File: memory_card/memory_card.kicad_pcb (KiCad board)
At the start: 2 copper layers, 100 x 100 mm, 22 parts, among them IC1 SN74HCT138N, IC2 SN74HCT138N, J1 Conn1, U1 AS6C4008, U2 74HCT374, U3 74HCT32, U4 74HCT00, U5 ZIF_AT28CXXX, U6 74HCT04, U7 74HCT374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

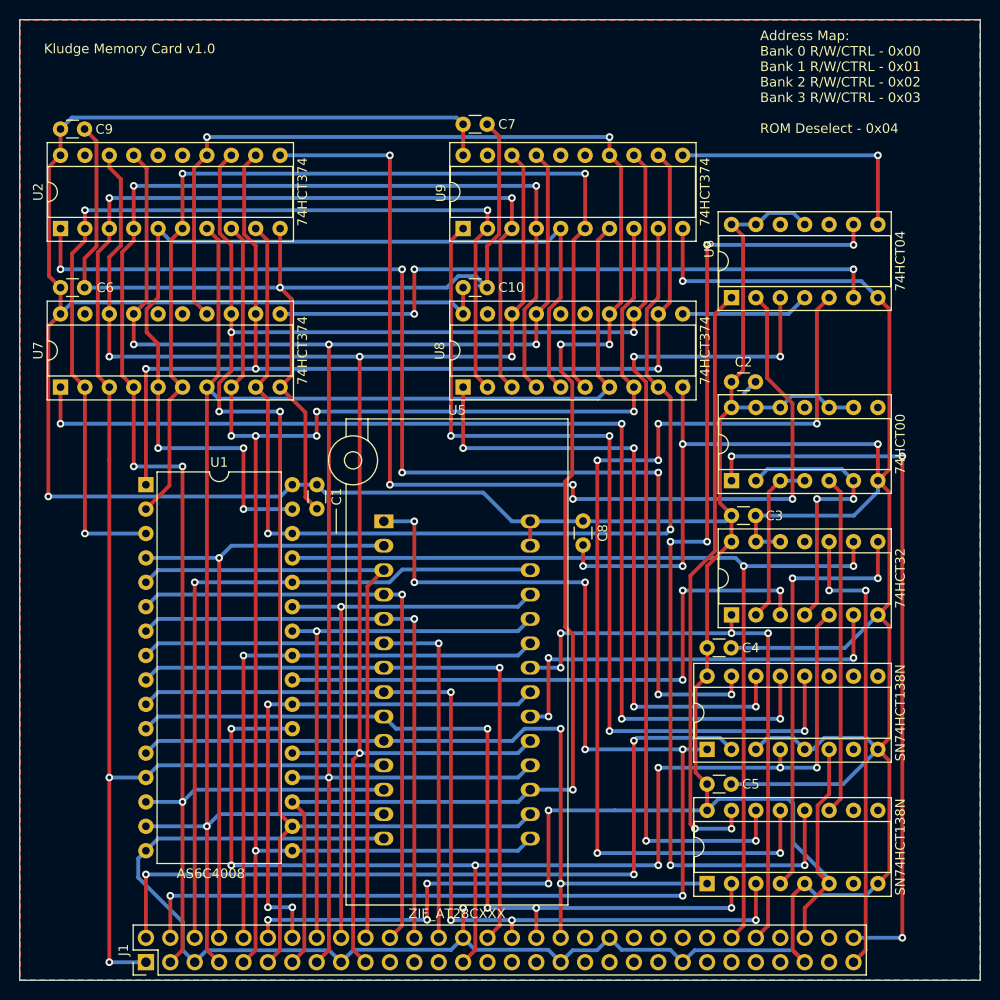
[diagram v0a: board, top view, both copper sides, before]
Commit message: Added missing decoupling capacitor to U6. Also reorganzied all decoupling capacitor's reference value to make it flow better on the PCB
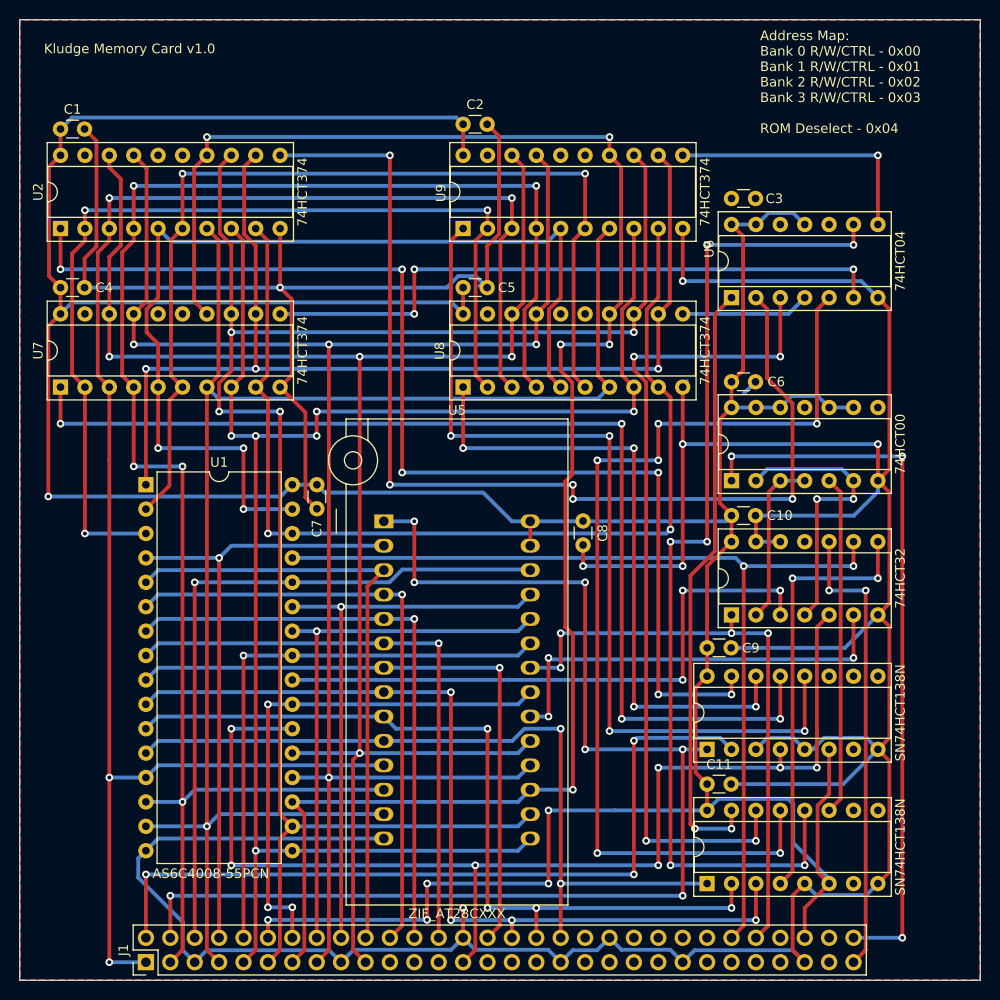
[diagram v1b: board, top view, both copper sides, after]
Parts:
- added C11: 100 nF, Capacitor_THT:C_Disc_D3.0mm_W1.6mm_P2.50mm, F.Cu at (174.0, 123.8)
- U1: value AS6C4008 -> AS6C4008-55PCN
- moved C9 86.3 mm to (174.0, 109.6)
- moved C4 77.1 mm to (106.7, 72.1)
- moved C6 70.5 mm to (176.6, 81.9)
- moved C5 57.6 mm to (148.6, 72.1)
- moved C1 45.6 mm to (106.7, 55.6), turned to 0 degrees
- moved C7 40.5 mm to (133.4, 92.7), turned to -90 degrees
- moved C2 38.7 mm to (148.6, 55.1)
- moved C10 36.7 mm to (176.6, 95.9)
- moved C3 33.0 mm to (176.6, 62.9)
